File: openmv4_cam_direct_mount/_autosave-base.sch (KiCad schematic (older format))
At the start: 63 parts, among them M1 9774030243R, M2 9774030243R, Q1 BSS138, Q2 Si2301BDS, U1 STM32H743VIT6, U2 OV7725, U5 TPS731XX, U8 PAM2305AABADJ, X1 MF-CON-MICROUSB-RIGHT, X2 USD-1040310811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

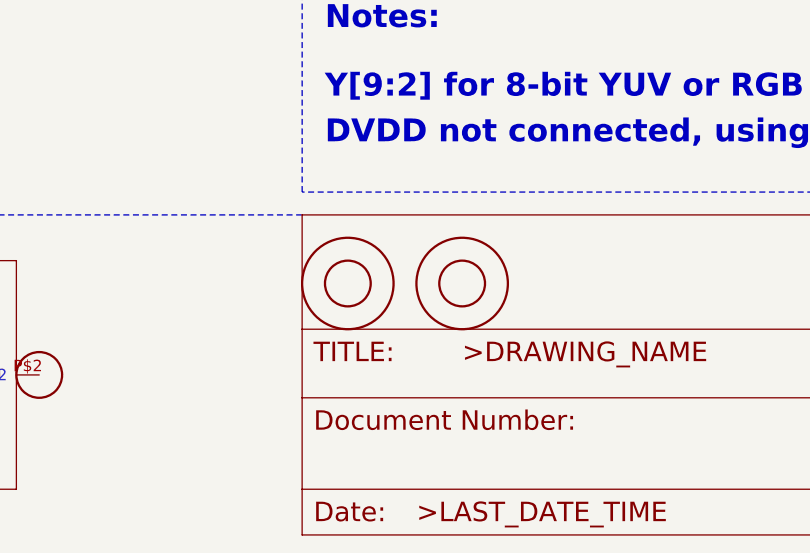
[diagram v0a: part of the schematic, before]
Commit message: Fixed camera mount hole links
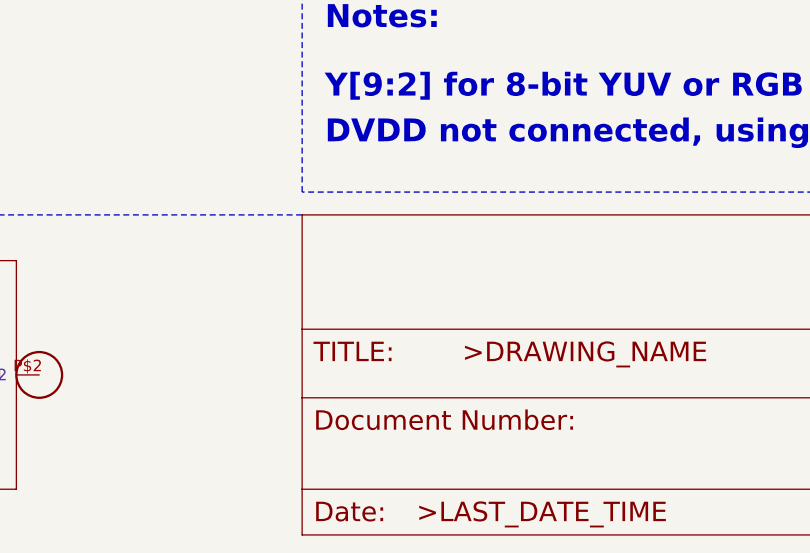
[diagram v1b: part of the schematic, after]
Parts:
- removed M1, M2: 9774030243R, base:9774030151R, symbol base-eagle-import:9774030151R
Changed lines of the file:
@@
-$EndComp
-$Comp
-L base-eagle-import:DINA3_L #FRAME1
-U 2 1 CC96BE8F
-P 15100 12900
-F 0 "#FRAME1" H 15100 12900 50  0001 C CNN
-F 1 "DINA3_L" H 15100 12900 50  0001 C CNN
-F 2 "" H 15100 12900 50  0001 C CNN
-F 3 "" H 15100 12900 50  0001 C CNN
-	2    15100 12900
-	1    0    0    -1
 $EndComp
 $Comp
@@
 F 3 "" H 18000 5200 50  0001 C CNN
 	1    18000 5200
-	1    0    0    -1
-$EndComp
-$Comp
-L base-eagle-import:9774030151R M1
-U 1 1 6705D9E8
-P 15800 11800
-F 0 "M1" H 15800 11800 50  0001 C CNN
-F 1 "9774030243R" H 15800 11800 50  0001 C CNN
-F 2 "base:9774030151R" H 15800 11800 50  0001 C CNN
-F 3 "" H 15800 11800 50  0001 C CNN
-	1    15800 11800
-	1    0    0    -1
-$EndComp
-$Comp
-L base-eagle-import:9774030151R M2
-U 1 1 29680FAA
-P 15300 11800
-F 0 "M2" H 15300 11800 50  0001 C CNN
-F 1 "9774030243R" H 15300 11800 50  0001 C CNN
-F 2 "base:9774030151R" H 15300 11800 50  0001 C CNN
-F 3 "" H 15300 11800 50  0001 C CNN
-	1    15300 11800
 	1    0    0    -1
 $EndComp
@@
 	1    0    0    -1
 $EndComp
+$Comp
+L base-eagle-import:DINA3_L #FRAME1
+U 2 1 CC96BE8F
+P 15100 12900
+F 0 "#FRAME1" H 15100 12900 50  0001 C CNN
+F 1 "DINA3_L" H 15100 12900 50  0001 C CNN
+F 2 "" H 15100 12900 50  0001 C CNN
+F 3 "" H 15100 12900 50  0001 C CNN
+	2    15100 12900
+	1    0    0    -1
+$EndComp
